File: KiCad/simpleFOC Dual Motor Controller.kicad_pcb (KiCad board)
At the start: 4 copper layers, 50 x 50 mm, 55 parts, among them CN101 MR60-F, CN201 MR60-F, CN601 MR60-F, Q301 AGM6014AP, Q303 AGM6014AP, Q401 AGM6014AP, Q403 AGM6014AP, Q501 AGM6014AP, Q503 AGM6014AP, Q701 AGM6014AP, Q703 AGM6014AP, Q801 AGM6014AP, Q803 AGM6014AP, Q901 AGM6014AP, Q903 AGM6014AP, U101 STM32F103C8Tx, U201 DRV8323HRTAT, U601 DRV8323HRTAT

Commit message: start adding control pins
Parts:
- removed CN101: MR60-F, easyeda2kicad:CONN-TH_3P-P5.50_MR60-F
- added R301: 47k, Resistor_SMD:R_0402_1005Metric, F.Cu at (148.6, 41.4)
- added R302: 47k, Resistor_SMD:R_0402_1005Metric, F.Cu at (143.4, 36.3)
- added R401: 47k, Resistor_SMD:R_0402_1005Metric, F.Cu at (141.6, 41.4)
- added R402: 47k, Resistor_SMD:R_0402_1005Metric, F.Cu at (136.3, 36.3)
- added R501: 47k, Resistor_SMD:R_0402_1005Metric, F.Cu at (133.9, 41.4)
- added R502: 47k, Resistor_SMD:R_0402_1005Metric, F.Cu at (128.8, 36.3)
- added R701: 47k, Resistor_SMD:R_0402_1005Metric, F.Cu at (114.6, 41.6)
- added R702: 47k, Resistor_SMD:R_0402_1005Metric, F.Cu at (109.3, 36.6)
- added R801: 47k, Resistor_SMD:R_0402_1005Metric, F.Cu at (106.9, 41.7)
- added R802: 47k, Resistor_SMD:R_0402_1005Metric, F.Cu at (101.8, 36.6)
- added R901: 47k, Resistor_SMD:R_0402_1005Metric, F.Cu at (121.6, 41.6)
- added R902: 47k, Resistor_SMD:R_0402_1005Metric, F.Cu at (116.4, 36.6)
- added U102: XT60H-M, easyeda2kicad:CONN-TH_XT60H-M, F.Cu at (133.7, 70.4)
- NT601, NT602, NT603: moved to B.Cu
- moved C601 103.1 mm to (120.7, 55.8), turned to -90 degrees
- moved U101 94.5 mm to (119.0, 67.8)
- moved U601 94.3 mm to (114.3, 54.2), turned to 180 degrees
- moved C602 93.1 mm to (118.9, 55.6), turned to -90 degrees
- moved C603 92.3 mm to (118.1, 58.1)
- moved C604 91.2 mm to (112.6, 58.6), turned to 180 degrees
- moved C605 89.0 mm to (110.0, 54.0), turned to -90 degrees
- moved R602 83.7 mm to (109.0, 54.9), turned to 90 degrees
- moved R601 82.7 mm to (108.0, 54.9), turned to 90 degrees
- moved C701 64.8 mm to (116.6, 45.8), turned to -90 degrees
- moved Rsns701 61.4 mm to (112.9, 45.9), turned to -90 degrees
- moved Q701 58.4 mm to (109.8, 39.1), turned to 180 degrees
- moved Q703 57.8 mm to (113.4, 39.1)
- moved NT603 47.0 mm to (111.0, 51.7), turned to -90 degrees
- moved Q901 46.2 mm to (117.0, 39.1), turned to 180 degrees
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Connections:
- C604 pad 2: GND -> /Motor Driver 1/Motor_VIN
- C605 pad 2: GND -> /Motor Driver 1/Motor_VIN
- NT601 pad 2: GND -> /Motor Driver 1/Motor_VIN
- NT602 pad 2: GND -> /Motor Driver 1/Motor_VIN
- NT603 pad 2: GND -> /Motor Driver 1/Motor_VIN
- Rsns401 pad 2: GND -> /Motor Driver 1/Motor_VIN
- Rsns701 pad 2: GND -> /Motor Driver 1/Motor_VIN
- Rsns901 pad 2: GND -> /Motor Driver 1/Motor_VIN
- U201 pad 21: unconnected-(U201-SOC-Pad21) -> /Motor Driver 1/SOC
- U201 pad 22: unconnected-(U201-SOB-Pad22) -> /Motor Driver 1/SOB
- U201 pad 23: unconnected-(U201-SOA-Pad23) -> /Motor Driver 1/SOA
- U201 pad 25: unconnected-(U201-nFAULT-Pad25) -> /Motor Driver 1/FAULT
- U201 pad 30: unconnected-(U201-ENABLE-Pad30) -> /Motor Driver 1/EN
- U201 pad 31: unconnected-(U201-CAL-Pad31) -> /Motor Driver 1/CAL
- U201 pad 34: unconnected-(U201-INHA-Pad34) -> /Motor Driver 1/INHA
- U201 pad 35: unconnected-(U201-INLA-Pad35) -> /Motor Driver 1/INLA
- U201 pad 36: unconnected-(U201-INHB-Pad36) -> /Motor Driver 1/INHB
- U201 pad 37: unconnected-(U201-INLB-Pad37) -> /Motor Driver 1/INLB
- U201 pad 38: unconnected-(U201-INHC-Pad38) -> /Motor Driver 1/INHC
- U201 pad 39: unconnected-(U201-INLC-Pad39) -> /Motor Driver 1/INLC
- U201 pad 40: GND -> /Motor Driver 1/Motor_VIN
- U201 pad 41: GND -> /Motor Driver 1/Motor_VIN
- U601 pad 21: unconnected-(U601-SOC-Pad21) -> /Motor Driver 2/SOC
- U601 pad 22: unconnected-(U601-SOB-Pad22) -> /Motor Driver 2/SOB
- U601 pad 23: unconnected-(U601-SOA-Pad23) -> /Motor Driver 2/SOA
- U601 pad 25: unconnected-(U601-nFAULT-Pad25) -> /Motor Driver 2/FAULT
- U601 pad 26: GND -> /Motor Driver 1/Motor_VIN
- U601 pad 30: unconnected-(U601-ENABLE-Pad30) -> /Motor Driver 2/EN
- U601 pad 31: unconnected-(U601-CAL-Pad31) -> /Motor Driver 2/CAL
- U601 pad 32: GND -> /Motor Driver 1/Motor_VIN
- U601 pad 34: unconnected-(U601-INHA-Pad34) -> /Motor Driver 2/INHA
- U601 pad 35: unconnected-(U601-INLA-Pad35) -> /Motor Driver 2/INLA
- U601 pad 36: unconnected-(U601-INHB-Pad36) -> /Motor Driver 2/INHB
- U601 pad 37: unconnected-(U601-INLB-Pad37) -> /Motor Driver 2/INLB
- U601 pad 38: unconnected-(U601-INHC-Pad38) -> /Motor Driver 2/INHC
- U601 pad 39: unconnected-(U601-INLC-Pad39) -> /Motor Driver 2/INLC
- U601 pad 40: GND -> /Motor Driver 1/Motor_VIN
- U601 pad 41: GND -> /Motor Driver 1/Motor_VIN
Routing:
- net /Motor Driver 1/Motor_VIN: track 14.7 -> 168.9 mm, vias 70 -> 193
- net /Motor Driver 2/Pole 3/GH: track 0.00 -> 27.4 mm, vias 0 -> 2
- net /Motor Driver 2/Pole 1/GH: track 0.00 -> 21.1 mm, vias 0 -> 2
- net /Motor Driver 2/Pole 2/GH: track 0.00 -> 20.0 mm
- net /Motor Driver 2/Pole 3/PoleOut: track 0.00 -> 19.1 mm, vias 0 -> 2
- net /Motor Driver 2/Pole 1/PoleOut: track 0.00 -> 18.7 mm, vias 0 -> 2
- net /Motor Driver 2/Pole 1/GL: track 0.00 -> 16.2 mm
- net /Motor Driver 2/Pole 3/GL: track 0.00 -> 15.0 mm
- net /Motor Driver 2/Pole 2/PoleOut: track 0.00 -> 13.6 mm, vias 0 -> 2
- net /Motor Driver 2/Pole 3/SP: track 0.00 -> 13.4 mm, vias 0 -> 2
- net /Motor Driver 2/Pole 1/SP: track 0.00 -> 12.6 mm, vias 0 -> 2
- net /Motor Driver 2/Pole 2/GL: track 0.00 -> 11.2 mm
- net /Motor Driver 2/Pole 2/SP: track 0.00 -> 10.6 mm, vias 0 -> 2
- net Net-(U601-SNB): track 0.00 -> 6.16 mm, vias 0 -> 1
- net Net-(U601-SNA): track 0.00 -> 5.06 mm, vias 0 -> 1
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- added copper zone on F.Cu, net /Motor Driver 2/Pole 1/PoleOut
- added copper zone on F.Cu, net /Motor Driver 2/Pole 1/SP
- added copper zone on F.Cu, net /Motor Driver 2/Pole 2/PoleOut
- added copper zone on F.Cu, net /Motor Driver 2/Pole 2/SP
- added copper zone on F.Cu, net /Motor Driver 2/Pole 3/PoleOut
- added copper zone on F.Cu, net /Motor Driver 2/Pole 3/SP

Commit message: not sure why the schematic and pcb aren't syncing :(
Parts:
- added J101: Conn_01x04, PCM_SparkFun-Connector:JST_1x04_P2.0mm_Vertical_PTH, F.Cu at (120.1, 72.1)
- added SW101: TS-1088-AR02016, easyeda2kicad:SW-SMD_L3.9-W3.0-P4.45, F.Cu at (111.0, 65.7)
- moved D101 56.3 mm to (137.4, 64.3), turned to 180 degrees
- moved D103 49.3 mm to (122.9, 67.1), turned to -90 degrees
- moved D104 45.4 mm to (120.4, 67.1), turned to 90 degrees
- moved U101 11.3 mm to (127.8, 60.7), turned to 90 degrees
- moved C601 0.31 mm to (121.0, 55.7)
- moved C602 0.31 mm to (119.2, 55.4)
- moved C603 0.31 mm to (118.4, 58.0)
- moved C604 0.31 mm to (112.9, 58.5)
- moved C605 0.31 mm to (110.3, 53.8)
- moved C701 0.31 mm to (116.9, 45.7)
- moved C801 0.31 mm to (102.2, 45.7)
- moved C901 0.31 mm to (109.7, 45.7)
- moved CN601 0.31 mm to (111.8, 30.8)
- moved NT601 0.31 mm to (120.1, 48.7)
- moved NT602 0.31 mm to (112.8, 48.3)
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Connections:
- C201 pad 1: /Motor Driver 1/Motor_VIN -> M+
- C202 pad 1: /Motor Driver 1/Motor_VIN -> M+
- C204 pad 2: /Motor Driver 1/Motor_VIN -> GND
- C205 pad 2: /Motor Driver 1/Motor_VIN -> GND
- C301 pad 1: /Motor Driver 1/Motor_VIN -> M+
- C401 pad 1: /Motor Driver 1/Motor_VIN -> M+
- C501 pad 1: /Motor Driver 1/Motor_VIN -> M+
- D101 pad 1: /Motor Driver 1/Motor_VIN -> M+
- NT201 pad 2: /Motor Driver 1/Motor_VIN -> GND
- NT202 pad 2: /Motor Driver 1/Motor_VIN -> GND
- NT203 pad 2: /Motor Driver 1/Motor_VIN -> GND
- Q301 pad 5: /Motor Driver 1/Motor_VIN -> M+
- Q401 pad 5: /Motor Driver 1/Motor_VIN -> M+
- Q501 pad 5: /Motor Driver 1/Motor_VIN -> M+
- Rsns301 pad 2: /Motor Driver 1/Motor_VIN -> GND
- Rsns401 pad 2: /Motor Driver 1/Motor_VIN -> GND
- U101 pad 10: unconnected-(U101-PA0-Pad10) -> /snsA2
- U101 pad 11: unconnected-(U101-PA1-Pad11) -> /snsB2
- U101 pad 12: unconnected-(U101-PA2-Pad12) -> /snsC2
- U101 pad 13: unconnected-(U101-PA3-Pad13) -> /CHAn2
- U101 pad 14: unconnected-(U101-PA4-Pad14) -> /snsA1
- U101 pad 15: unconnected-(U101-PA5-Pad15) -> /snsB1
- U101 pad 16: unconnected-(U101-PA6-Pad16) -> /snsC1
- U101 pad 17: unconnected-(U101-PA7-Pad17) -> /CHCn1
- U101 pad 18: unconnected-(U101-PB0-Pad18) -> /CHBn1
- U101 pad 19: unconnected-(U101-PB1-Pad19) -> /CHAn1
- U101 pad 21: unconnected-(U101-PB10-Pad21) -> /ctrl_scl
- U101 pad 22: unconnected-(U101-PB11-Pad22) -> /ctrl_sda
- U101 pad 26: unconnected-(U101-PB13-Pad26) -> /sns_sck
- U101 pad 27: unconnected-(U101-PB14-Pad27) -> /sns_miso
- U101 pad 28: unconnected-(U101-PB15-Pad28) -> /sns_mosi
- U101 pad 29: unconnected-(U101-PA8-Pad29) -> /CHA1
- U101 pad 30: unconnected-(U101-PA9-Pad30) -> /CHB1
- U101 pad 31: unconnected-(U101-PA10-Pad31) -> /CHC1
- U101 pad 32: unconnected-(U101-PA11-Pad32) -> /sns_cs1
- U101 pad 33: unconnected-(U101-PA12-Pad33) -> /sns_cs2
- U101 pad 34: unconnected-(U101-PA13-Pad34) -> /SWDIO
- U101 pad 37: unconnected-(U101-PA14-Pad37) -> /SWCLK
- U101 pad 38: unconnected-(U101-PA15-Pad38) -> /CHA2
- U101 pad 39: unconnected-(U101-PB3-Pad39) -> /SWO
- U101 pad 40: unconnected-(U101-PB4-Pad40) -> /CHB2
- U101 pad 41: unconnected-(U101-PB5-Pad41) -> /CHBn2
- U101 pad 42: unconnected-(U101-PB6-Pad42) -> /CHC2
- U101 pad 43: unconnected-(U101-PB7-Pad43) -> /CHCn2
- U101 pad 7: unconnected-(U101-NRST-Pad7) -> /~{rst}
- U102 pad 2: /Motor Driver 1/Motor_VIN -> M+
- U201 pad 21: /Motor Driver 1/SOC -> /snsC1
- U201 pad 22: /Motor Driver 1/SOB -> /snsB1
- U201 pad 23: /Motor Driver 1/SOA -> /snsA1
- U201 pad 26: /Motor Driver 1/Motor_VIN -> GND
- U201 pad 32: /Motor Driver 1/Motor_VIN -> GND
- U201 pad 34: /Motor Driver 1/INHA -> /CHA1
- U201 pad 35: /Motor Driver 1/INLA -> /CHAn1
- U201 pad 36: /Motor Driver 1/INHB -> /CHB1
- U201 pad 37: /Motor Driver 1/INLB -> /CHBn1
- U201 pad 38: /Motor Driver 1/INHC -> /CHC1
- U201 pad 39: /Motor Driver 1/INLC -> /CHCn1
- U201 pad 4: /Motor Driver 1/Motor_VIN -> M+
- U201 pad 40: /Motor Driver 1/Motor_VIN -> GND
- U201 pad 41: /Motor Driver 1/Motor_VIN -> GND
- U201 pad 5: /Motor Driver 1/Motor_VIN -> M+
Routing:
- net /Motor Driver 1/Motor_VIN: track 168.9 -> 84.1 mm, vias 193 -> 22
- net GND: track 0.00 -> 74.7 mm, vias 193 -> 293
- net M+: track 0.00 -> 10.1 mm, vias 0 -> 71
- added copper zone on F.Cu, net M+
- added copper zone on In2.Cu, net M+
- removed copper zone on F.Cu, net /Motor Driver 1/Motor_VIN
- removed copper zone on In2.Cu, net /Motor Driver 1/Motor_VIN

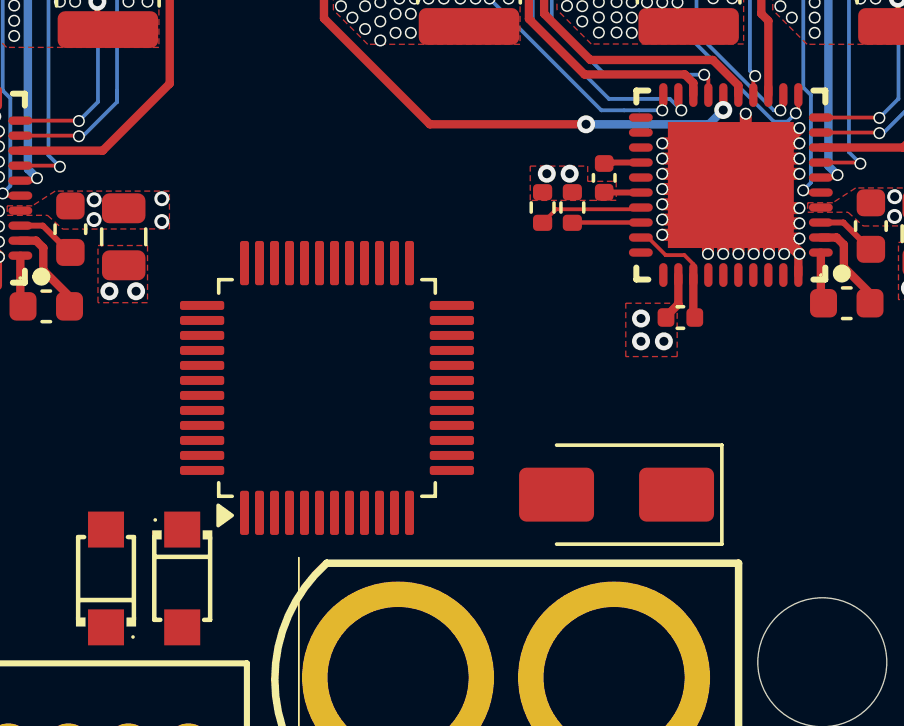
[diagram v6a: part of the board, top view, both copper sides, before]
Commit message: connected a few more signals
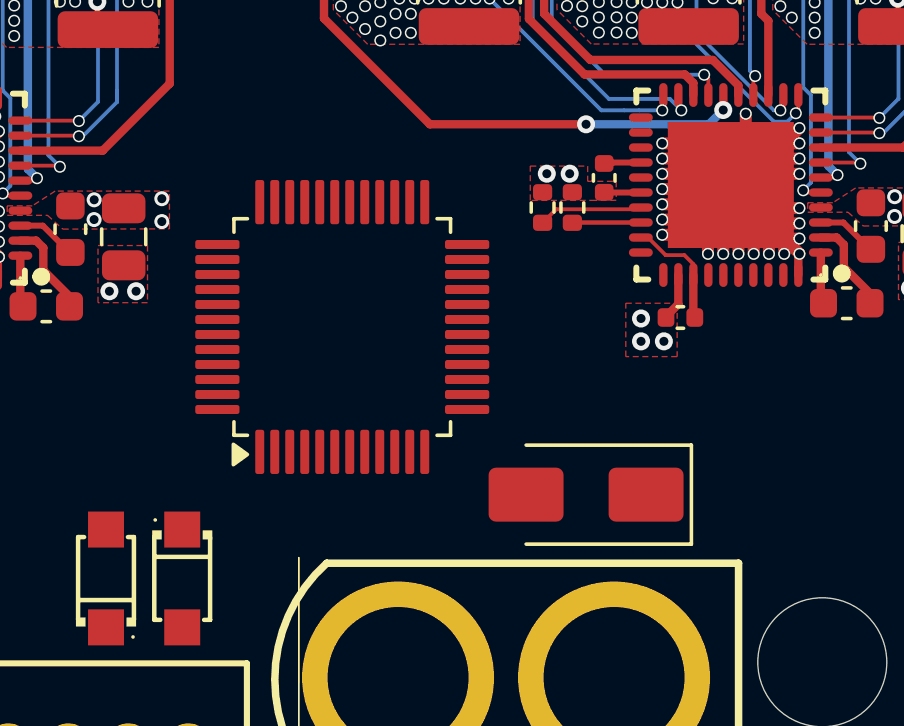
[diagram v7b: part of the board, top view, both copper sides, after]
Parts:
- moved U101 2.09 mm to (128.3, 58.7)
- moved D101 1.02 mm to (136.4, 64.3)

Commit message: condensed
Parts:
- removed C601: 100n, Capacitor_SMD:C_0805_2012Metric
- removed C602: 1u, Capacitor_SMD:C_0603_1608Metric
- removed C603: 47n, Capacitor_SMD:C_0603_1608Metric
- removed C604: 1u, Capacitor_SMD:C_0402_1005Metric
- removed C605: 0.1u, Capacitor_SMD:C_0402_1005Metric
- removed C701, C801, C901: 10u, Capacitor_SMD:C_1206_3216Metric
- removed CN601: MR60-F, easyeda2kicad:CONN-TH_3P-P5.50_MR60-F
- removed NT601, NT602, NT603: NetTie_2, CustomNetTie:NetTie0.127mm
- removed Q701, Q703, Q801, Q803, Q901, Q903: AGM6014AP, easyeda2kicad:PDFN-8_L3.1-W3.0-P0.65-LS3.3-BL
- removed R601, R602: 75k, Resistor_SMD:R_0402_1005Metric
- removed R701, R702, R801, R802, R901, R902: 47k, Resistor_SMD:R_0402_1005Metric
- removed Rsns701, Rsns801, Rsns901: 0.001, Resistor_SMD:R_2512_6332Metric
- removed U601: DRV8323HRTAT, easyeda2kicad:WQFN-40_L6.0-W6.0-P0.50-TL-EP4.2
- added C108: 10u, Capacitor_SMD:C_1206_3216Metric, F.Cu at (116.8, 42.0)
- added C109: 10u, Capacitor_SMD:C_1206_3216Metric, F.Cu at (102.2, 42.0)
- added C110: 10u, Capacitor_SMD:C_1206_3216Metric, F.Cu at (109.6, 42.0)
- added C206: 100n, Capacitor_SMD:C_0805_2012Metric, F.Cu at (120.6, 53.3)
- added C207: 1u, Capacitor_SMD:C_0603_1608Metric, F.Cu at (118.8, 53.0)
- added C208: 47n, Capacitor_SMD:C_0603_1608Metric, F.Cu at (118.8, 56.0)
- added C209: 0.1u, Capacitor_SMD:C_0402_1005Metric, F.Cu at (110.1, 50.5)
- added C210: 1u, Capacitor_SMD:C_0402_1005Metric, F.Cu at (112.2, 55.9)
- added C401: 10u, Capacitor_SMD:C_1206_3216Metric, F.Cu at (124.9, 31.4)
- added C401: 10u, Capacitor_SMD:C_1206_3216Metric, F.Cu at (124.9, 29.0)
- added C401: 10u, Capacitor_SMD:C_1206_3216Metric, F.Cu at (124.9, 38.8)
- added C401: 10u, Capacitor_SMD:C_1206_3216Metric, F.Cu at (124.9, 43.7)
- added C401: 10u, Capacitor_SMD:C_1206_3216Metric, F.Cu at (124.9, 26.6)
- added C401: 10u, Capacitor_SMD:C_1206_3216Metric, F.Cu at (124.9, 33.9)
- added C401: 10u, Capacitor_SMD:C_1206_3216Metric, F.Cu at (124.9, 41.2)
- added C401: 10u, Capacitor_SMD:C_1206_3216Metric, F.Cu at (124.9, 36.4)
- added CN202: MR60-F, easyeda2kicad:CONN-TH_3P-P5.50_MR60-F, F.Cu at (111.3, 30.2)
- added NT204: NetTie_2, CustomNetTie:NetTie0.127mm, B.Cu at (119.7, 46.3)
- added NT205: NetTie_2, CustomNetTie:NetTie0.127mm, B.Cu at (112.5, 46.0)
- added NT206: NetTie_2, CustomNetTie:NetTie0.127mm, B.Cu at (110.8, 49.2)
- added Q101: AGM6014AP, easyeda2kicad:PDFN-8_L3.1-W3.0-P0.65-LS3.3-BL, F.Cu at (116.8, 37.4)
- added Q102: AGM6014AP, easyeda2kicad:PDFN-8_L3.1-W3.0-P0.65-LS3.3-BL, F.Cu at (109.6, 37.4)
- added Q103: AGM6014AP, easyeda2kicad:PDFN-8_L3.1-W3.0-P0.65-LS3.3-BL, F.Cu at (102.2, 37.4)
- added Q104: AGM6014AP, easyeda2kicad:PDFN-8_L3.1-W3.0-P0.65-LS3.3-BL, F.Cu at (120.5, 37.4)
- added Q105: AGM6014AP, easyeda2kicad:PDFN-8_L3.1-W3.0-P0.65-LS3.3-BL, F.Cu at (113.3, 37.4)
- added Q106: AGM6014AP, easyeda2kicad:PDFN-8_L3.1-W3.0-P0.65-LS3.3-BL, F.Cu at (105.8, 37.4)
- added R101: 47k, Resistor_SMD:R_0402_1005Metric, F.Cu at (116.9, 46.3)
- added R102: 47k, Resistor_SMD:R_0402_1005Metric, F.Cu at (109.6, 46.2)
- added R103: 47k, Resistor_SMD:R_0402_1005Metric, F.Cu at (102.2, 46.2)
- added R104: 47k, Resistor_SMD:R_0402_1005Metric, F.Cu at (116.9, 45.2)
- added R105: 47k, Resistor_SMD:R_0402_1005Metric, F.Cu at (109.6, 45.2)
- added R106: 47k, Resistor_SMD:R_0402_1005Metric, F.Cu at (102.2, 45.2)
- added R203: 100k, Resistor_SMD:R_0402_1005Metric, F.Cu at (139.6, 57.1)
- added R204: 100k, Resistor_SMD:R_0402_1005Metric, F.Cu at (141.5, 56.1)
- added R205: 100k, Resistor_SMD:R_0402_1005Metric, F.Cu at (141.5, 57.1)
- added R206: 100k, Resistor_SMD:R_0402_1005Metric, F.Cu at (143.4, 57.1)
- added R207: 100k, Resistor_SMD:R_0402_1005Metric, F.Cu at (143.4, 56.1)
- added R208: 100k, Resistor_SMD:R_0402_1005Metric, F.Cu at (144.8, 56.8)
- added R209: 100k, Resistor_SMD:R_0402_1005Metric, F.Cu at (137.5, 54.6)
- added R210: 100k, Resistor_SMD:R_0402_1005Metric, F.Cu at (136.4, 54.6)
- added R211: 100k, Resistor_SMD:R_0402_1005Metric, F.Cu at (136.5, 50.7)
- added R212: 75k, Resistor_SMD:R_0402_1005Metric, F.Cu at (110.1, 52.4)
- added R213: 75k, Resistor_SMD:R_0402_1005Metric, F.Cu at (109.1, 52.4)
- added R214: 100k, Resistor_SMD:R_0402_1005Metric, F.Cu at (112.2, 56.9)
- added R215: 100k, Resistor_SMD:R_0402_1005Metric, F.Cu at (114.1, 55.9)
- added R216: 100k, Resistor_SMD:R_0402_1005Metric, F.Cu at (114.1, 56.9)
- added R217: 100k, Resistor_SMD:R_0402_1005Metric, F.Cu at (116.0, 56.9)
- added R218: 100k, Resistor_SMD:R_0402_1005Metric, F.Cu at (116.0, 55.9)
- added R219: 100k, Resistor_SMD:R_0402_1005Metric, F.Cu at (117.4, 56.5)
- added R220: 100k, Resistor_SMD:R_0402_1005Metric, F.Cu at (110.1, 54.4)
- added R221: 100k, Resistor_SMD:R_0402_1005Metric, F.Cu at (109.1, 54.4)
- added R222: 100k, Resistor_SMD:R_0402_1005Metric, F.Cu at (109.1, 50.5)
- added Rsns101: 0.001, Resistor_SMD:R_2512_6332Metric, F.Cu at (120.1, 43.4)
- added Rsns102: 0.001, Resistor_SMD:R_2512_6332Metric, F.Cu at (112.7, 43.4)
- added Rsns103: 0.001, Resistor_SMD:R_2512_6332Metric, F.Cu at (105.4, 43.4)
- added U202: DRV8323HRTAT, easyeda2kicad:WQFN-40_L6.0-W6.0-P0.50-TL-EP4.2, F.Cu at (114.1, 51.7)
- moved R302 10.3 mm to (144.3, 46.6)
- moved R502 10.2 mm to (129.5, 46.5)
- moved R402 10.2 mm to (137.0, 46.5)
- moved R401 6.11 mm to (137.0, 45.4), turned to 0 degrees
- moved R301 5.90 mm to (144.3, 45.4), turned to 0 degrees
- moved R501 5.90 mm to (129.5, 45.4)
- moved C301 3.41 mm to (144.2, 42.2)
- moved C401 3.37 mm to (129.6, 42.3)
- moved C501 3.35 mm to (137.0, 42.3)
- moved C205 2.99 mm to (137.5, 50.7), turned to 90 degrees
- moved R201 2.53 mm to (136.4, 52.7)
- moved R202 2.53 mm to (137.4, 52.7)
- moved C204 2.22 mm to (139.6, 56.1)
- moved NT202 2.07 mm to (139.9, 46.2)
- moved C201 2.05 mm to (148.0, 53.5)
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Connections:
- U101 pad 25: unconnected-(U101-PB12-Pad25) -> /FAULT1
- U101 pad 3: unconnected-(U101-PC14-Pad3) -> /FAULT2
- U101 pad 45: unconnected-(U101-PB8-Pad45) -> /EN1
- U101 pad 46: unconnected-(U101-PB9-Pad46) -> /CAL1
- U101 pad 5: unconnected-(U101-PD0-Pad5) -> /EN2
- U101 pad 6: unconnected-(U101-PD1-Pad6) -> /CAL2
- U201 pad 25: /Motor Driver 1/FAULT -> /Motor Driver 1/~{FAULT}
- U201 pad 30: /Motor Driver 1/EN -> /EN1
- U201 pad 31: /Motor Driver 1/CAL -> /CAL1
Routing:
- net /Motor Driver 1/Motor_VIN: track 84.1 -> 0.00 mm, vias 22 -> 0
- net GND: track 74.7 -> 146.8 mm, vias 293 -> 220
- net /Motor Driver 1/Pole 2/PoleOut: track 13.6 -> 28.3 mm, vias 2 -> 4
- net /Motor Driver 2/Pole 2/PoleOut: track 13.6 -> 28.3 mm, vias 2 -> 4
- net /Motor Driver 2/Pole 3/PoleOut: track 19.1 -> 32.7 mm, vias 2 -> 4
- net /Motor Driver 1/Pole 3/PoleOut: track 19.1 -> 32.7 mm, vias 2 -> 4
- net /Motor Driver 1/Pole 1/SP: track 12.6 -> 25.9 mm, vias 2 -> 4
- net /Motor Driver 2/Pole 1/SP: track 12.6 -> 25.9 mm, vias 2 -> 4
- net /Motor Driver 2/Pole 1/PoleOut: track 18.7 -> 30.6 mm, vias 2 -> 4
- net /Motor Driver 1/Pole 1/PoleOut: track 18.7 -> 30.6 mm, vias 2 -> 4
- net /Motor Driver 1/Pole 3/GL: track 15.0 -> 24.5 mm, vias 0 -> 2
- net /Motor Driver 2/Pole 3/GL: track 15.0 -> 24.5 mm, vias 0 -> 2
- net M+: track 10.1 -> 1.23 mm, vias 71 -> 106
- net /Motor Driver 1/Pole 2/GL: track 11.2 -> 19.7 mm, vias 0 -> 2
- net /Motor Driver 2/Pole 2/GL: track 11.2 -> 19.7 mm, vias 0 -> 2
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- removed copper zone on F.Cu, net /Motor Driver 2/Pole 1/PoleOut
- removed copper zone on B.Cu, net GND
